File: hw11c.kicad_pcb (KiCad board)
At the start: 2 copper layers, 49 x 27.5 mm, 88 parts, among them Q1 KX-7_12MHZ, SW1 BUTT1, SW2 BUTT2, X1 ~RESET, X10 PIO2.8, X11 PIO1.4, X12 ADC3, X13 PIO0.8, X14 PIO0.9, X15 MAT0, X16 PIO0.6, X17 PIO0.7, X18 ADC6, X2 SWCLK, X3 SWDIO, X4 SSEL1, X5 SCK1, X6 MISO1, X7 MOSI1, X8 PIO2.6, X9 PIO2.7

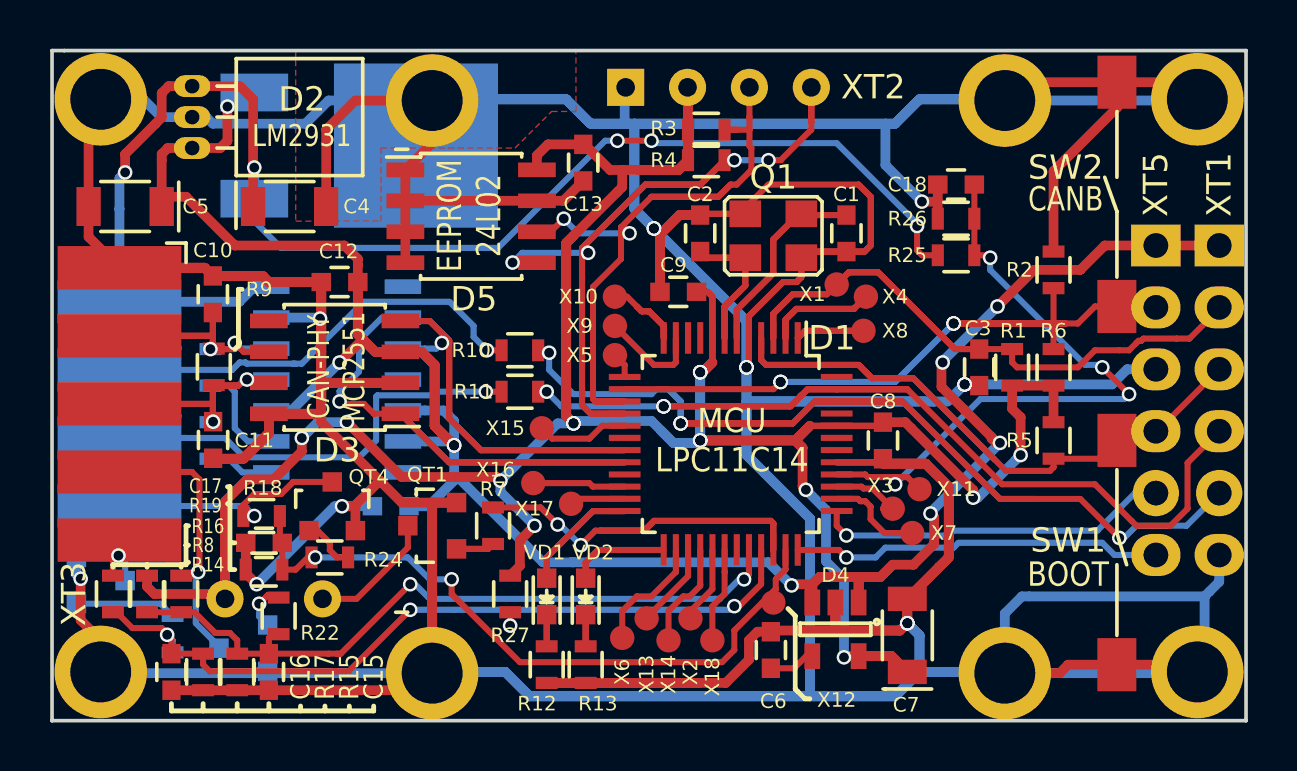
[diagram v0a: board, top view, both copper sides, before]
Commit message: Add Rs signal for MCP2551. Pin connected to MCU pin 3.4.
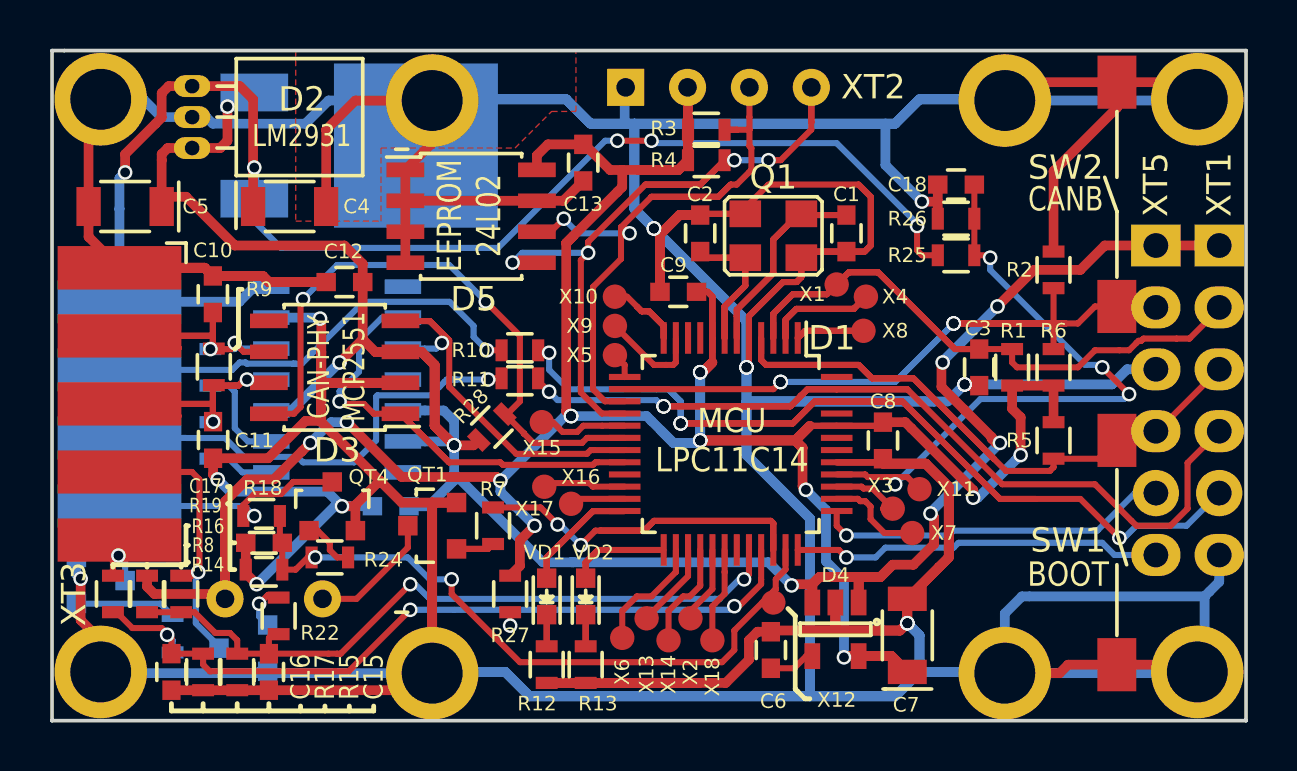
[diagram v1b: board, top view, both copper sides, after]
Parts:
- added R28: 10k, libs:R_0603, F.Cu at (68.0, 65.5)
- moved R11 0.55 mm to (69.1, 63.5)
- moved X16 0.47 mm to (70.1, 67.9)
- moved X15 0.25 mm to (70.0, 65.2)
- moved C12 0.20 mm to (61.9, 59.5)
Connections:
- D1 pad 18: Net-(D1-Pad18) -> /CAN_RS
- D3 pad 8: GND -> /CAN_RS
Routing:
- net /CAN_RS: track 0.00 -> 25.6 mm, vias 0 -> 2
- net /I2C_SDA: track 43.2 -> 30.7 mm
- net /CAN_RX: track 28.5 -> 17.0 mm
- net /3.3V: track 137.0 -> 128.5 mm
- net /CAN_TX: track 27.8 -> 20.7 mm
- net GND: track 501.2 -> 497.0 mm, vias 13 -> 14
- net /5V: track 103.4 -> 101.4 mm
- net /I2C_SCL: track 29.7 -> 28.1 mm
